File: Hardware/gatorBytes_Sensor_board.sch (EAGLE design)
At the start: 24 parts, among them U2 LIGHT_SENSORTEMT6000

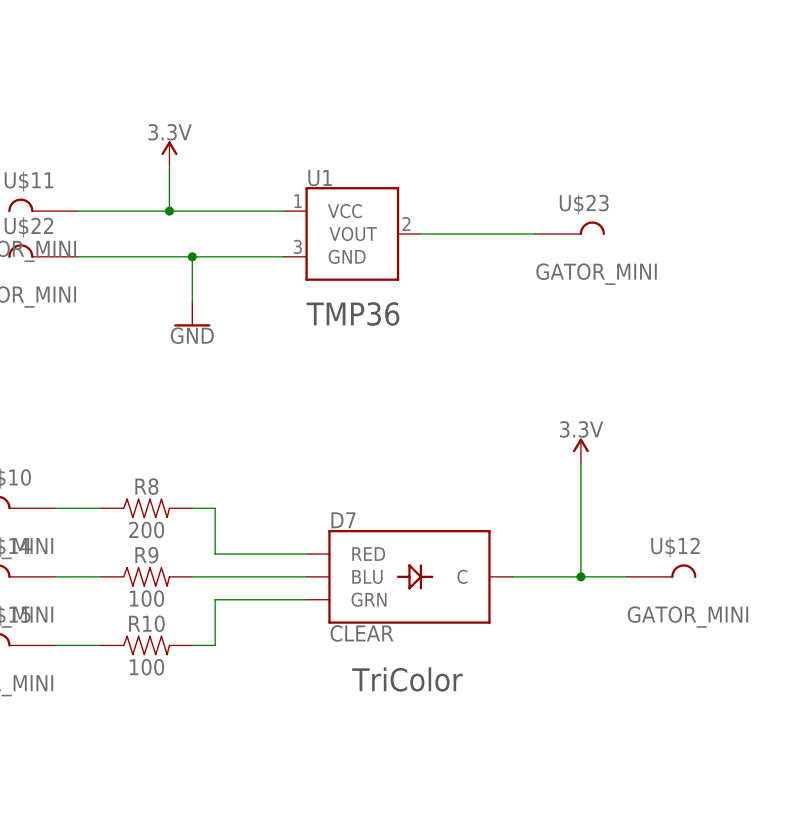
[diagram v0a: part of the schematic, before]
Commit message: removing pth
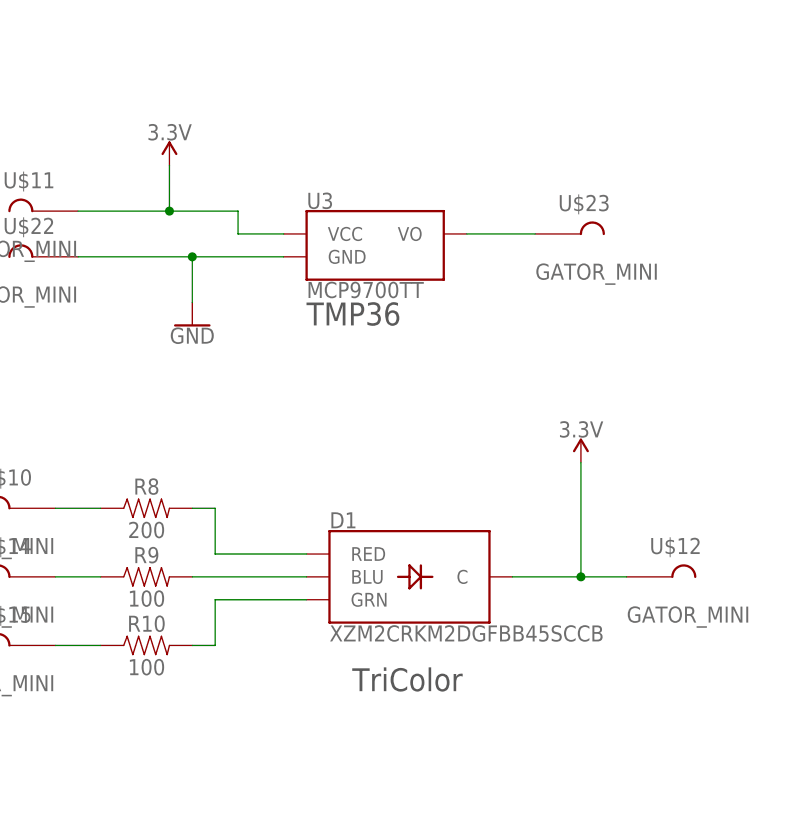
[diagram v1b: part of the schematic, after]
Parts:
- removed D7: CLEAR, SparkFun-LED:LED-RGB-CCCLEAR
- removed U1: (no value), SparkFun-Sensors:TMP36GT9-KIT
- added D1: XZM2CRKM2DGFBB45SCCB, SparkFun-LED:SUNLEDSMD1
- added U3: MCP9700TT, SparkFun-Sensors:MCP9700TT
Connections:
- net 3.3V: now also D1.C, U3.VCC; no longer D7.C, U1.VCC
- net GND: now also U3.GND; no longer U1.GND
- net N$10: now also U3.VO; no longer U1.VOUT
- net N$11: now also D1.BLU; no longer D7.BLU
- net N$12: now also D1.RED; no longer D7.RED
- net N$13: now also D1.GRN; no longer D7.GRN
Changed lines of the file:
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@@
 <?xml version="1.0" encoding="utf-8"?>
 <!DOCTYPE eagle SYSTEM "eagle.dtd">
-<eagle version="8.7.0">
+<eagle version="9.1.0">
 <drawing>
 <settings>
@@
 <parts>
 <part name="FRAME1" library="SparkFun-Aesthetics" deviceset="FRAME-LETTER" device=""/>
-<part name="D7" library="SparkFun-LED" deviceset="LED-RGB-CC" device="CLEAR" value="CLEAR"/>
 <part name="R8" library="SparkFun-Resistors" deviceset="200OHM" device="-0603-1/10W-1%" value="200"/>
 <part name="R9" library="SparkFun-Resistors" deviceset="100OHM" device="-0603-1/4W-5%" value="100"/>
@@
 <part name="U$14" library="TAB" deviceset="GATOR_MINI" device=""/>
 <part name="U$15" library="TAB" deviceset="GATOR_MINI" device=""/>
-<part name="U1" library="SparkFun-Sensors" deviceset="TMP36" device="GT9-KIT"/>
 <part name="U$11" library="TAB" deviceset="GATOR_MINI" device=""/>
 <part name="U$22" library="TAB" deviceset="GATOR_MINI" device=""/>
@@
 <part name="LOGO1" library="SparkFun-Aesthetics" library_urn="urn:adsk.eagle:library:507" deviceset="SFE_LOGO_FLAME" device=".1_INCH" package3d_urn="urn:adsk.eagle:package:37114/1"/>
 <part name="LOGO2" library="SparkFun-Aesthetics" library_urn="urn:adsk.eagle:library:507" deviceset="OSHW-LOGO" device="S" package3d_urn="urn:adsk.eagle:package:37099/1"/>
+<part name="U3" library="SparkFun-Sensors" deviceset="MCP9700" device="TT"/>
+<part name="D1" library="SparkFun-LED" deviceset="SUNLED" device="SMD1" value="XZM2CRKM2DGFBB45SCCB"/>
 </parts>
 <sheets>
@@
 <instance part="FRAME1" gate="G$1" x="0" y="0"/>
 <instance part="FRAME1" gate="V" x="147.32" y="0"/>
-<instance part="D7" gate="G$1" x="58.42" y="114.3"/>
 <instance part="R8" gate="G$1" x="30.48" y="121.92"/>
 <instance part="R9" gate="G$1" x="30.48" y="114.3"/>
@@
 <instance part="U$14" gate="G$1" x="17.78" y="114.3" rot="MR0"/>
 <instance part="U$15" gate="G$1" x="17.78" y="106.68" rot="MR0"/>
-<instance part="U1" gate="G$1" x="53.34" y="152.4"/>
 <instance part="U$11" gate="G$1" x="20.32" y="154.94" rot="MR0"/>
 <instance part="U$22" gate="G$1" x="20.32" y="149.86" rot="MR0"/>
@@
 <instance part="LOGO1" gate="G$1" x="147.32" y="38.1"/>
 <instance part="LOGO2" gate="G$1" x="170.18" y="45.72"/>
+<instance part="U3" gate="G$1" x="55.88" y="149.86"/>
+<instance part="D1" gate="G1" x="58.42" y="114.3"/>
 </instances>
 <busses>
@@
 <net name="3.3V" class="0">
 <segment>
-<pinref part="D7" gate="G$1" pin="C"/>
 <wire x1="71.12" y1="114.3" x2="78.74" y2="114.3" width="0.1524" layer="91"/>
 <wire x1="78.74" y1="114.3" x2="78.74" y2="127" width="0.1524" layer="91"/>
@@
 <junction x="78.74" y="114.3"/>
 <pinref part="U$12" gate="G$1" pin="P$1"/>
+<pinref part="D1" gate="G1" pin="C"/>
 </segment>
 <segment>
 <pinref part="U$11" gate="G$1" pin="P$1"/>
-<pinref part="U1" gate="G$1" pin="VCC"/>
 <wire x1="22.86" y1="154.94" x2="33.02" y2="154.94" width="0.1524" layer="91"/>
 <pinref part="SUPPLY10" gate="G$1" pin="3.3V"/>
-<wire x1="33.02" y1="154.94" x2="45.72" y2="154.94" width="0.1524" layer="91"/>
 <wire x1="33.02" y1="160.02" x2="33.02" y2="154.94" width="0.1524" layer="91"/>
+<wire x1="33.02" y1="154.94" x2="40.64" y2="154.94" width="0.1524" layer="91"/>
 <junction x="33.02" y="154.94"/>
+<wire x1="40.64" y1="154.94" x2="40.64" y2="152.4" width="0.1524" layer="91"/>
+<pinref part="U3" gate="G$1" pin="VCC"/>
+<wire x1="40.64" y1="152.4" x2="45.72" y2="152.4" width="0.1524" layer="91"/>
 </segment>
 <segment>
@@
 <segment>
 <pinref part="U$22" gate="G$1" pin="P$1"/>
-<pinref part="U1" gate="G$1" pin="GND"/>
 <wire x1="22.86" y1="149.86" x2="35.56" y2="149.86" width="0.1524" layer="91"/>
 <pinref part="GND9" gate="1" pin="GND"/>
@@
 <wire x1="35.56" y1="144.78" x2="35.56" y2="149.86" width="0.1524" layer="91"/>
 <junction x="35.56" y="149.86"/>
+<pinref part="U3" gate="G$1" pin="GND"/>
 </segment>
 <segment>
@@
 <net name="N$11" class="0">
 <segment>
-<pinref part="D7" gate="G$1" pin="BLU"/>
 <pinref part="R9" gate="G$1" pin="2"/>
 <wire x1="48.26" y1="114.3" x2="35.56" y2="114.3" width="0.1524" layer="91"/>
+<pinref part="D1" gate="G1" pin="BLU"/>
 </segment>
 </net>
 <net name="N$12" class="0">
 <segment>
-<pinref part="D7" gate="G$1" pin="RED"/>
 <wire x1="48.26" y1="116.84" x2="38.1" y2="116.84" width="0.1524" layer="91"/>
 <wire x1="38.1" y1="116.84" x2="38.1" y2="121.92" width="0.1524" layer="91"/>
 <pinref part="R8" gate="G$1" pin="2"/>
 <wire x1="38.1" y1="121.92" x2="35.56" y2="121.92" width="0.1524" layer="91"/>
+<pinref part="D1" gate="G1" pin="RED"/>
 </segment>
 </net>
 <net name="N$13" class="0">
 <segment>
-<pinref part="D7" gate="G$1" pin="GRN"/>
 <wire x1="48.26" y1="111.76" x2="38.1" y2="111.76" width="0.1524" layer="91"/>
 <wire x1="38.1" y1="111.76" x2="38.1" y2="106.68" width="0.1524" layer="91"/>
 <pinref part="R10" gate="G$1" pin="2"/>
 <wire x1="38.1" y1="106.68" x2="35.56" y2="106.68" width="0.1524" layer="91"/>
+<pinref part="D1" gate="G1" pin="GRN"/>
 </segment>
 </net>
@@
 <net name="N$10" class="0">
 <segment>
-<pinref part="U1" gate="G$1" pin="VOUT"/>
 <pinref part="U$23" gate="G$1" pin="P$1"/>
-<wire x1="60.96" y1="152.4" x2="73.66" y2="152.4" width="0.1524" layer="91"/>
-</segment>
-</net>
+<pinref part="U3" gate="G$1" pin="VO"/>
+<wire x1="66.04" y1="152.4" x2="73.66" y2="152.4" width="0.1524" layer="91"/>
+</segment>
+</net>

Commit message: adding new tabs
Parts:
- added U$19, U$35: GATOR_MINI, TAB:GATOR_MINI
- D1: device SparkFun-LED:SUNLEDSMD1 -> SparkFun-LED:LED-RGB-CASMD
- U$10, U$14, U$15, U$23, U$24: value GATOR_MINI -> GATOR; device TAB:GATOR_MINI -> SparkFun-Connectors:GATOR
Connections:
- net 3.3V: now also D1.A, U$19.P$1; no longer D1.C
- net GND: now also U$35.P$1

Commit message: post checklist chanegs
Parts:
- D1: device SparkFun-LED:LED-RGB-CASMD -> SparkFun-LED:SUNLEDSMD1
- U$11, U$12, U$19, U$22, U$25, U$26, U$35: value GATOR_MINI -> TAB_GATOR_MINI; device TAB:GATOR_MINI -> SparkFun-Connectors:TAB_GATOR_MINI
- U$23: value GATOR -> TAB_GATOR_MINI; device SparkFun-Connectors:GATOR -> SparkFun-Connectors:TAB_GATOR_MINI
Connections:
- net 3.3V: no longer D1.A, U$12.P$1
- net GND: now also D1.C, U$12.P$1
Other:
- note added: "MCP9700 Temperature Sensor"
- note added: "Power"
- note added: "RGB LED"
- note added: "v10"
- note removed: "TMP36"
- note removed: "TriColor"
- note removed: "v01"
- moved on the sheet: R10, R11, R8, R9, U$10, U$11, U$12, U$14, U$15, U$19, U$22, U$23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

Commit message: post qc checklist
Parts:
- added LOGO7: REVISION, SparkFun-Aesthetics:REVISION
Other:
- note added: "A. England"
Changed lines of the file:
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@@
 <part name="U$35" library="SparkFun-Connectors" deviceset="TAB_GATOR_MINI" device=""/>
 <part name="GND2" library="SparkFun-PowerSymbols" deviceset="GND" device=""/>
+<part name="LOGO7" library="SparkFun-Aesthetics" deviceset="REVISION" device=""/>
 </parts>
 <sheets>
@@
 <wire x1="0" y1="55.88" x2="147.32" y2="55.88" width="0.1524" layer="97" style="longdash"/>
 <text x="71.12" y="114.3" size="2.54" layer="97" font="vector" ratio="15">Power</text>
+<text x="169.164" y="6.858" size="2.54" layer="94" font="vector" ratio="15">A. England</text>
 </plain>
 <instances>
@@
 <instance part="U$35" gate="G$1" x="71.12" y="127"/>
 <instance part="GND2" gate="1" x="93.98" y="17.78"/>
+<instance part="LOGO7" gate="G$1" x="148.59" y="7.112"/>
 </instances>
 <busses>

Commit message: silk update
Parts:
- U$23: value TAB_GATOR_MINI -> GATOR; device SparkFun-Connectors:TAB_GATOR_MINI -> SparkFun-Connectors:GATOR
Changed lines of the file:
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@@
 <part name="U$11" library="SparkFun-Connectors" deviceset="TAB_GATOR_MINI" device=""/>
 <part name="U$22" library="SparkFun-Connectors" deviceset="TAB_GATOR_MINI" device=""/>
-<part name="U$23" library="SparkFun-Connectors" deviceset="TAB_GATOR_MINI" device=""/>
+<part name="U$23" library="SparkFun-Connectors" deviceset="GATOR" device=""/>
 <part name="SUPPLY10" library="SparkFun-PowerSymbols" deviceset="3.3V" device=""/>
 <part name="GND9" library="SparkFun-PowerSymbols" deviceset="GND" device=""/>
